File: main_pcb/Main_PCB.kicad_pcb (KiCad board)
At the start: 2 copper layers, 95 x 95 mm, 50 parts, among them J1 DBG, J2 UI, J3 UI, J4 Raspberry_Pi_2_3, J5 UI, J6 UI, J7 UPDN, J8 ISP, Q1 BSS123, Q2 HSS2307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

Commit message: Added I2C connection between pi and avr, just in case
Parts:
- added R3: 10k, Resistor_SMD:R_0603_1608Metric, F.Cu at (131.0, 73.5)
- added R4: 10k, Resistor_SMD:R_0603_1608Metric, F.Cu at (128.4, 73.5)
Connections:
- J4 pad 3: Net-(J4-Pad3) -> /SDA
- J4 pad 5: Net-(J4-Pad5) -> /SCL
- R12 pad 1: Net-(R12-Pad1) -> Net-(J4-Pad31)
- U1 pad 15: Net-(R12-Pad1) -> Net-(J4-Pad31)
- U3 pad 26: Net-(U3-Pad26) -> /PWR_EN
- U3 pad 27: /PWR_EN -> /SDA
- U3 pad 28: Net-(U3-Pad28) -> /SCL

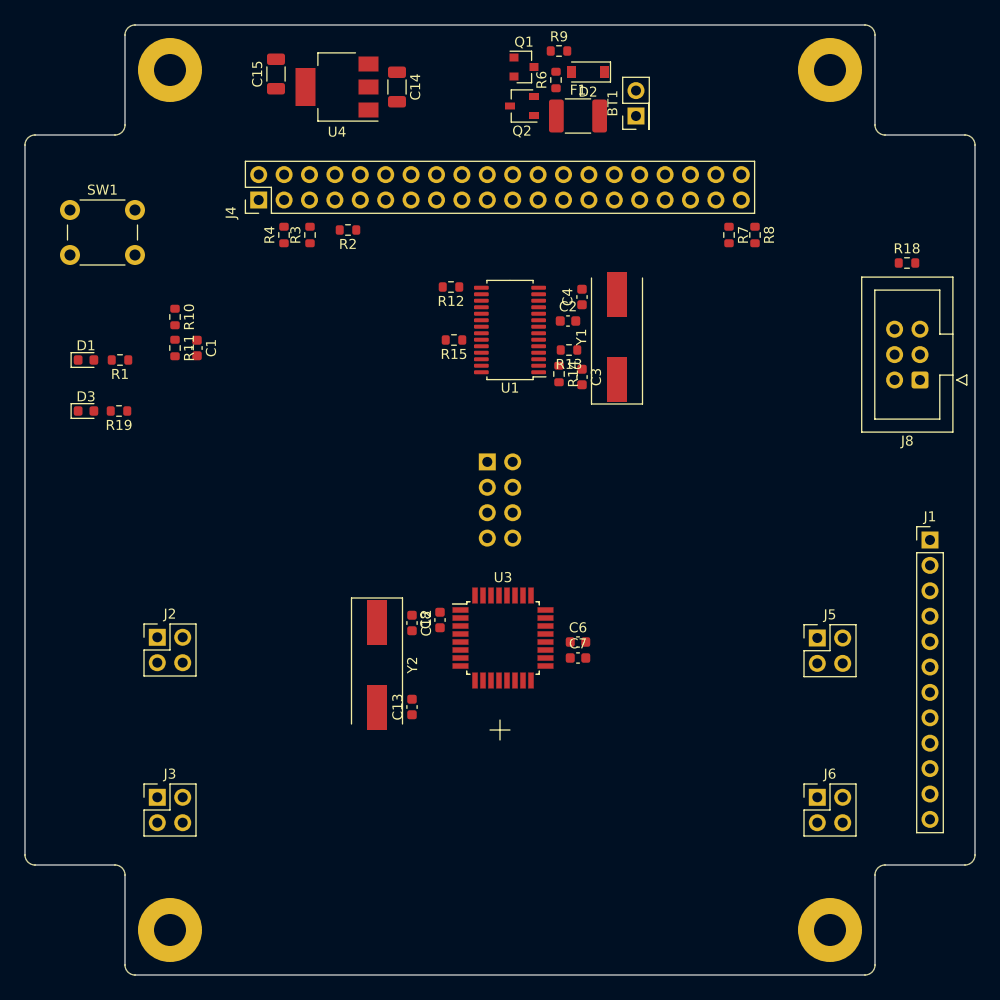
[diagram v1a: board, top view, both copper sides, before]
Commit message: Intial routing of main pcb
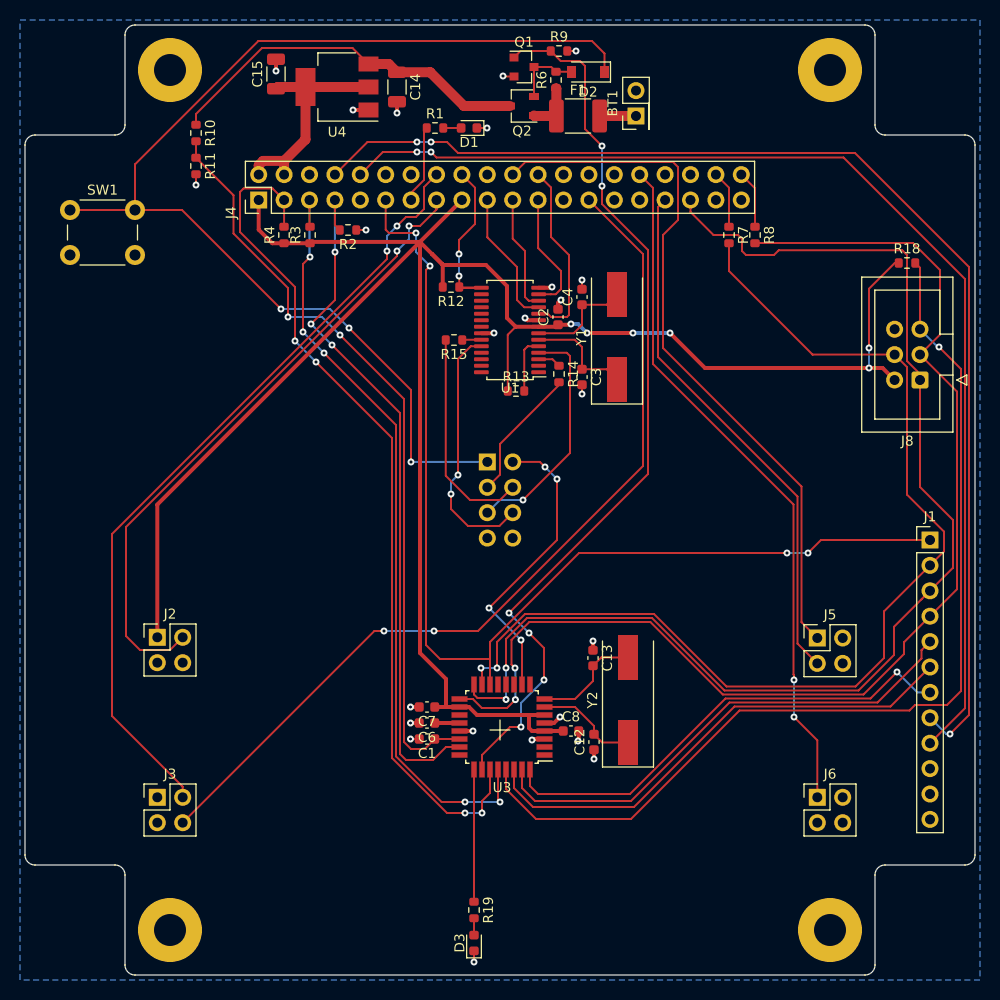
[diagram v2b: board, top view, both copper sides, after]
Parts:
- J4: value Raspberry_Pi_2_3 -> Raspberry_Pi_Zero_WH
- moved D3 65.8 mm to (147.4, 144.3), turned to 90 degrees
- moved R19 61.2 mm to (147.4, 141.0), turned to 270 degrees
- moved C1 45.4 mm to (142.7, 123.9), turned to 180 degrees
- moved D1 44.8 mm to (146.9, 62.8), turned to 180 degrees
- moved R1 39.1 mm to (143.5, 62.8), turned to 0 degrees
- moved Y2 25.3 mm to (162.8, 120.0), turned to 90 degrees
- moved C12 21.7 mm to (159.4, 124.2), turned to 90 degrees
- moved C13 18.8 mm to (159.3, 115.8), turned to 270 degrees
- moved R10 18.5 mm to (119.6, 63.3)
- moved R11 18.3 mm to (119.6, 66.6)
- moved C8 17.2 mm to (157.1, 123.1), turned to 0 degrees
- moved C6 17.1 mm to (142.7, 122.3), turned to 180 degrees
- moved C7 15.9 mm to (142.7, 120.7), turned to 180 degrees
- moved U3 8.90 mm to (150.2, 122.7), turned to 180 degrees
- moved R13 6.70 mm to (151.6, 89.1), turned to 0 degrees
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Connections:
- J3 pad 4: /TRIG -> /BTN_TRIG
- J4 pad 18: /STAT -> /~SC_IRQ
- J4 pad 27: Net-(J4-Pad27) -> /BTN_TRIG
- J4 pad 32: Net-(J4-Pad32) -> /BR-
- J4 pad 33: Net-(J4-Pad33) -> /STAT
- J4 pad 37: /BR- -> Net-(J4-Pad37)
- R12 pad 1: Net-(J4-Pad31) -> /~SC_IRQ
- U1 pad 15: Net-(J4-Pad31) -> /~SC_IRQ
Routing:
- net +3V3: track 0.00 -> 218.1 mm, vias 0 -> 6
- net /MISO: track 0.00 -> 124.7 mm, vias 0 -> 2
- net /PI_TXD: track 0.00 -> 120.1 mm, vias 0 -> 3
- net /SCK: track 0.00 -> 119.7 mm, vias 0 -> 2
- net /MASTER_ON: track 0.00 -> 115.4 mm, vias 0 -> 3
- net /PI_RXD: track 0.00 -> 114.5 mm, vias 0 -> 2
- net /MOSI: track 0.00 -> 107.6 mm, vias 0 -> 2
- net /SS: track 0.00 -> 107.5 mm, vias 0 -> 4
- net /~RESET: track 0.00 -> 98.8 mm, vias 0 -> 1
- net /PWR_EN: track 0.00 -> 91.4 mm, vias 0 -> 6
- net /BTN_TRIG: track 0.00 -> 89.6 mm, vias 0 -> 2
- net /SDA: track 0.00 -> 86.6 mm, vias 0 -> 4
- net /SP-: track 0.00 -> 79.2 mm, vias 0 -> 2
- net /SCL: track 0.00 -> 78.1 mm, vias 0 -> 5
- net /REF_BAT: track 0.00 -> 76.9 mm, vias 0 -> 2
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- added copper zone on B.Cu, net GND
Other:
- net class Default: trace_width 0.25 -> 0.2; via_dia 0.8 -> 0.7; via_drill 0.4 -> 0.3
- rule via_min_size: 0.4 -> 0.7

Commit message: Updated main pcb with power button in ui
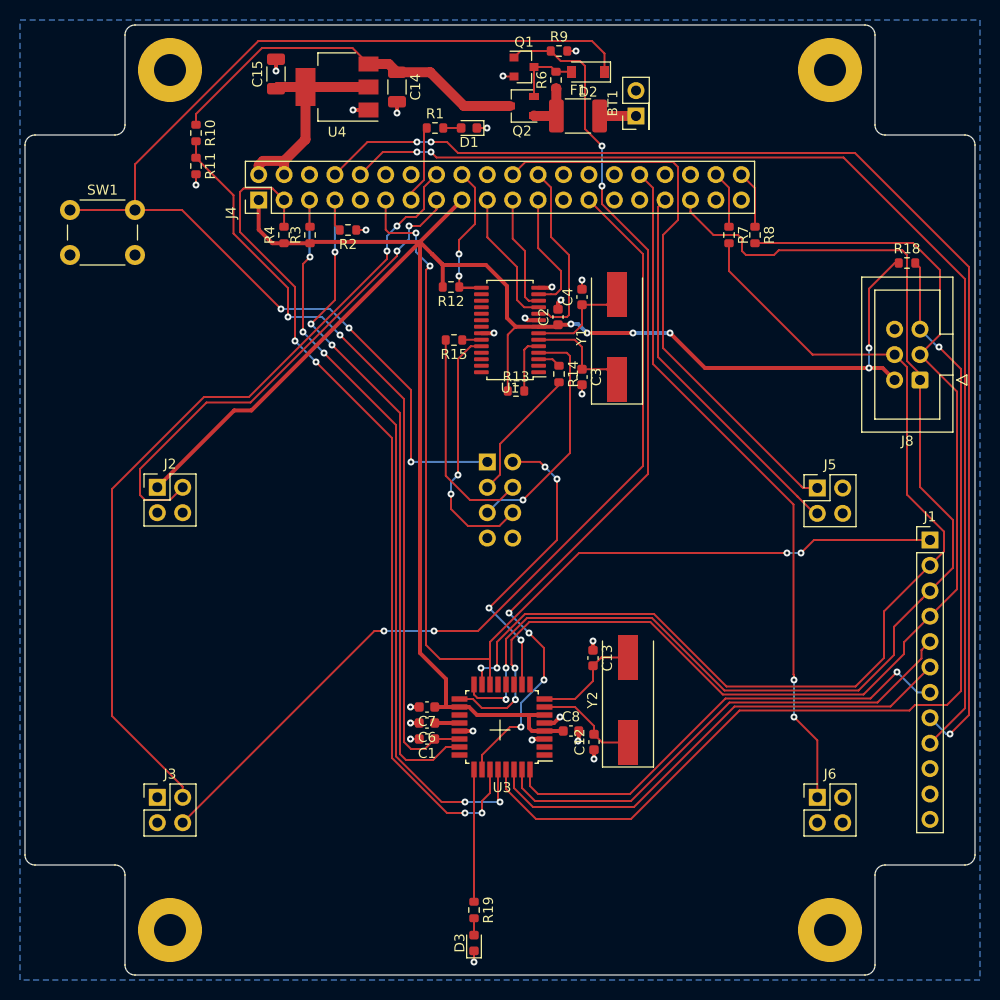
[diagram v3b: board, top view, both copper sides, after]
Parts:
- moved J2 15.0 mm to (115.7, 98.7)
- moved J5 15.0 mm to (181.7, 98.8)
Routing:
- net /STAT: track 53.2 -> 38.4 mm
- net /BR+: track 71.4 -> 57.2 mm
- net +3V3: track 218.1 -> 204.1 mm
- net /SP+: track 63.9 -> 50.0 mm
- net /SP-: track 79.2 -> 81.9 mm

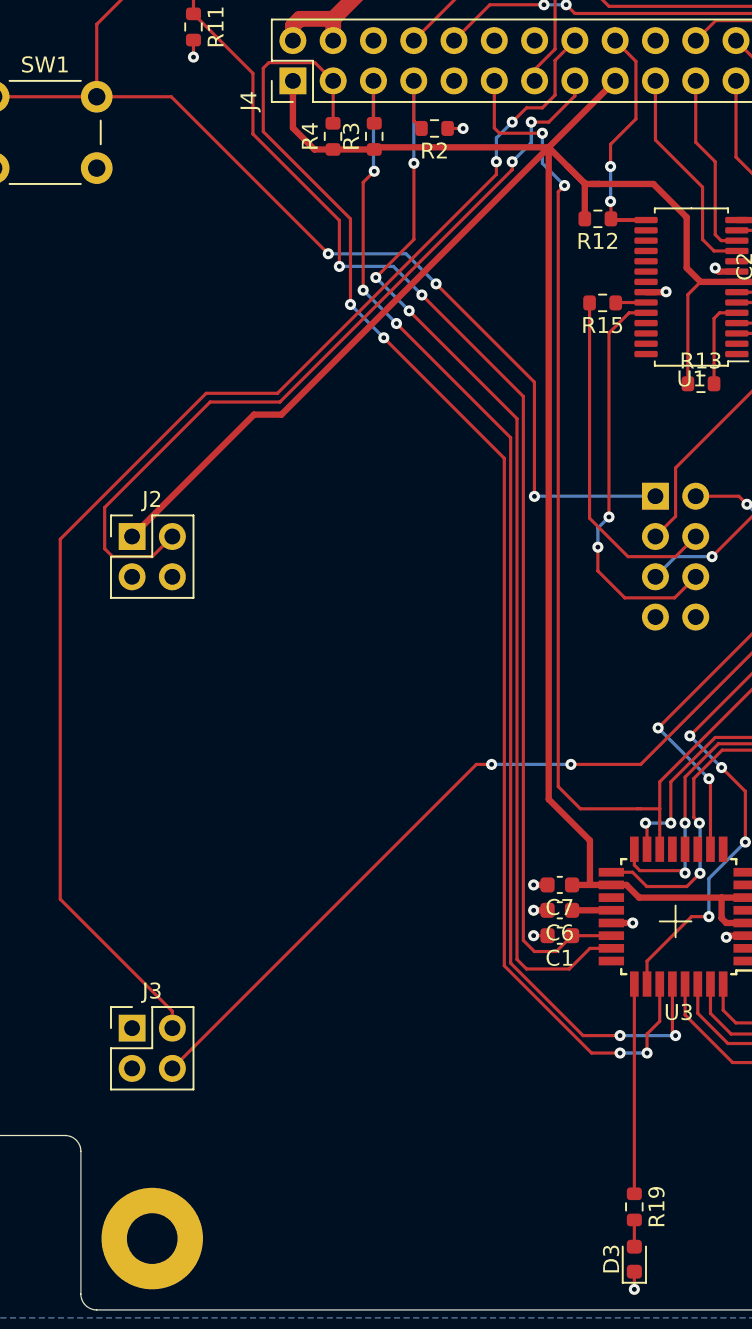
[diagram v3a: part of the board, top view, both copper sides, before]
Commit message: Added pin header for ui trigger button for external trigger button
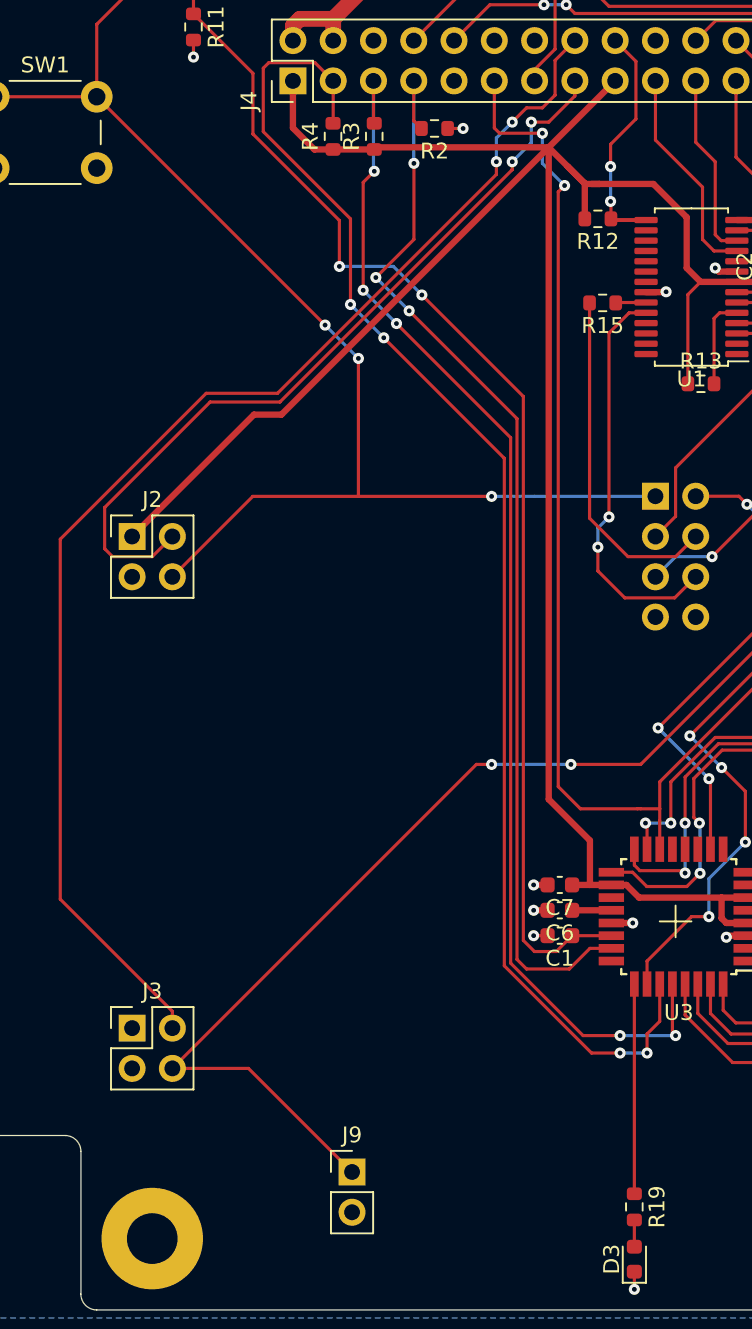
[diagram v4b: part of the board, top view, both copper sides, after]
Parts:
- added J9: BTN_TRIG, Connector_PinHeader_2.54mm:PinHeader_1x02_P2.54mm_Vertical, F.Cu at (129.6, 138.8)
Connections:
- J2 pad 4: GND -> /MASTER_ON
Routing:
- net /MASTER_ON: track 115.4 -> 130.1 mm
- net /BTN_TRIG: track 89.6 -> 103.7 mm

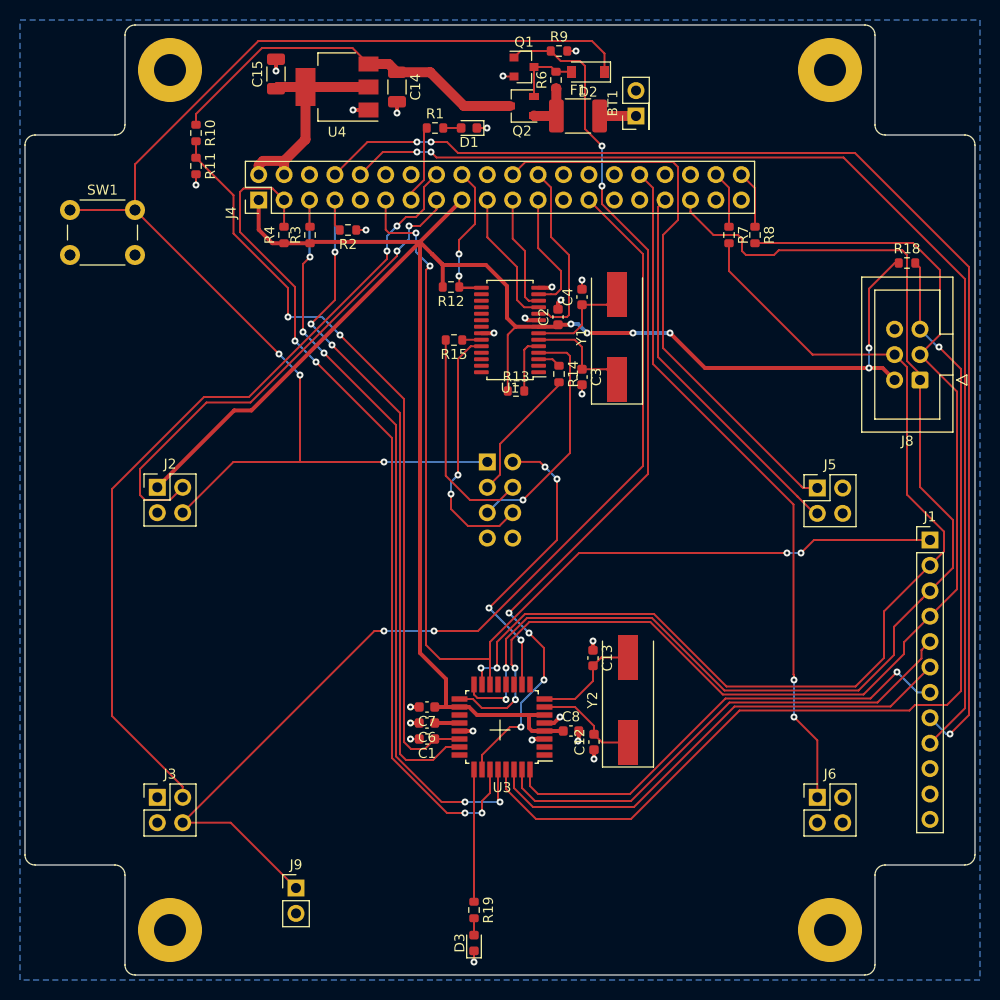
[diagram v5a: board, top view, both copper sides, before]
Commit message: Moved UI to avoid collision with RPi
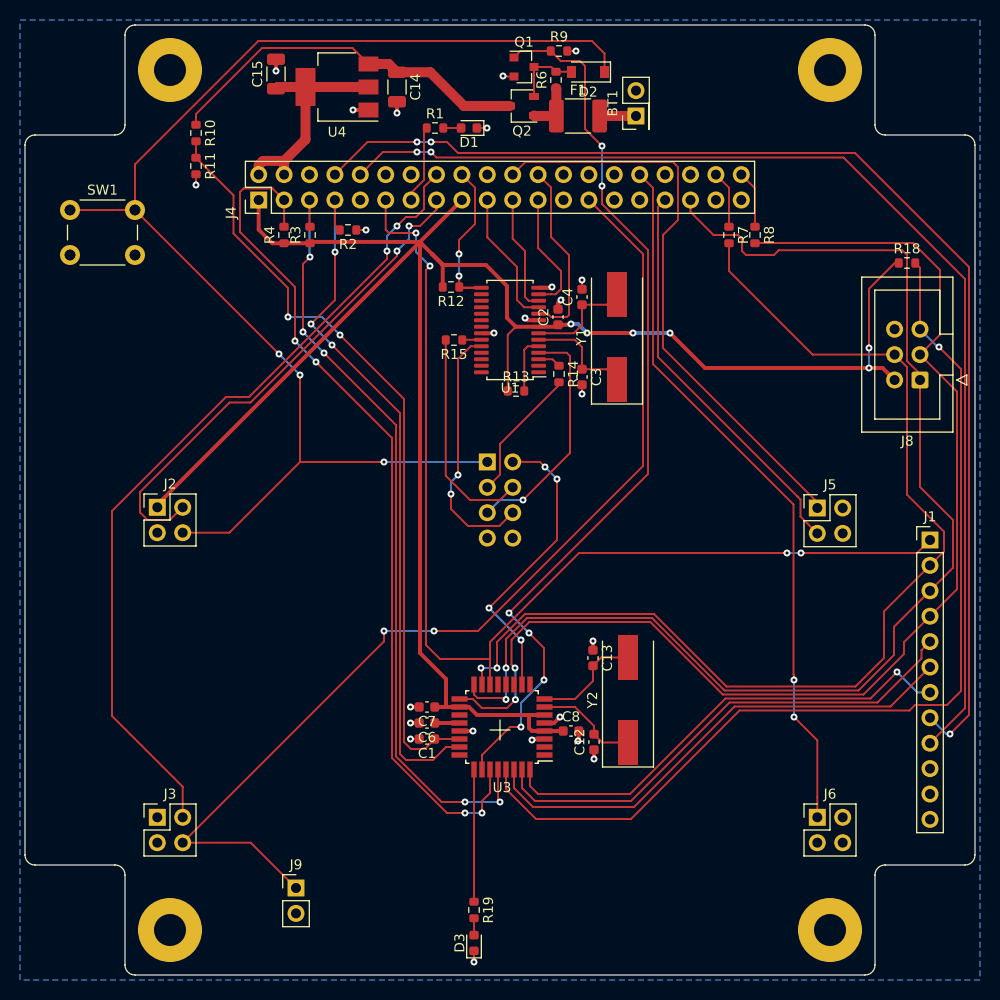
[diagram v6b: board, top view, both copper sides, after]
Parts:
- moved J2 2.00 mm to (115.7, 100.7)
- moved J3 2.00 mm to (115.7, 131.7)
- moved J5 2.00 mm to (181.7, 100.8)
- moved J6 2.00 mm to (181.7, 131.7)
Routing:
- net /BR-: track 69.6 -> 71.6 mm
- net /STAT: track 38.4 -> 40.2 mm
- net /BR+: track 57.2 -> 58.4 mm
- net +3V3: track 204.1 -> 205.1 mm
- net /MASTER_ON: track 130.1 -> 130.9 mm
- net /SP-: track 81.9 -> 82.6 mm
- net /BTN_TRIG: track 103.7 -> 104.3 mm
